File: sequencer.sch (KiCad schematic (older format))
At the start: 27 parts, among them J101 USB_A, J102 NHD-3.12-25664UC, J103 PJS008U-3000, U101 74HCT125, U102 74HC595, U103 74HC595, U104 74HC595, U105 74HC165

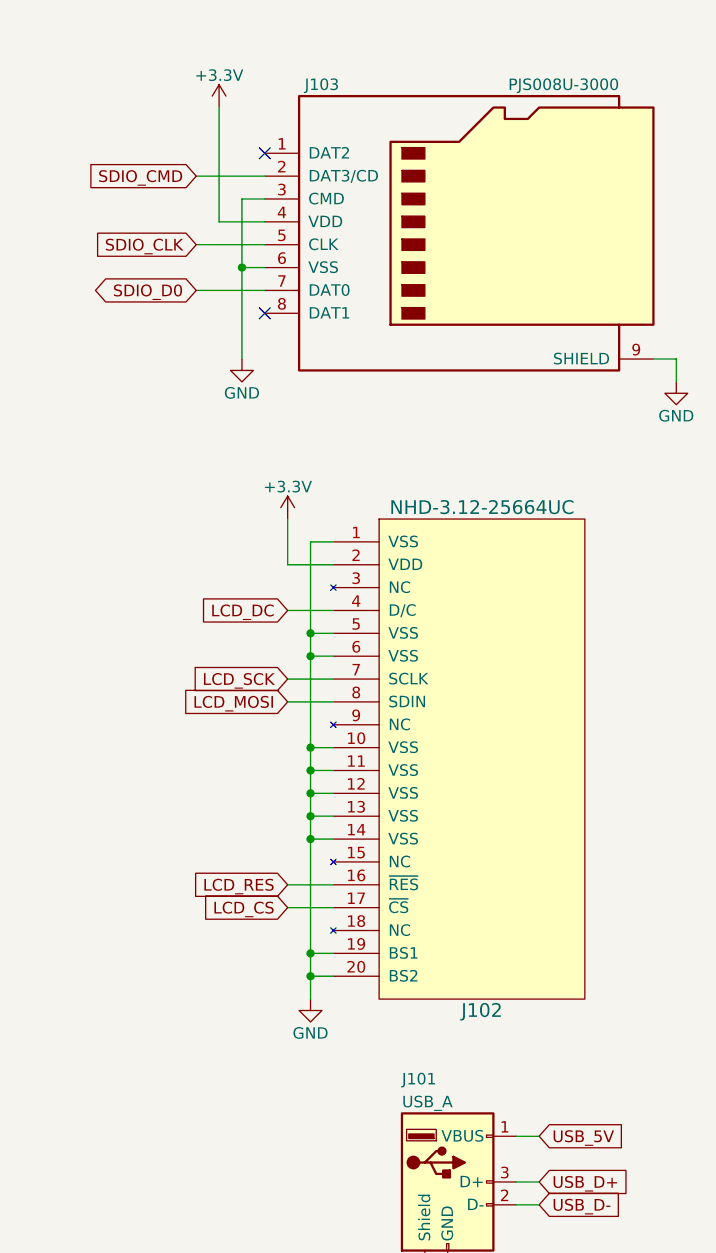
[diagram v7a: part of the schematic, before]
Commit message: renamed header references to JPxxx
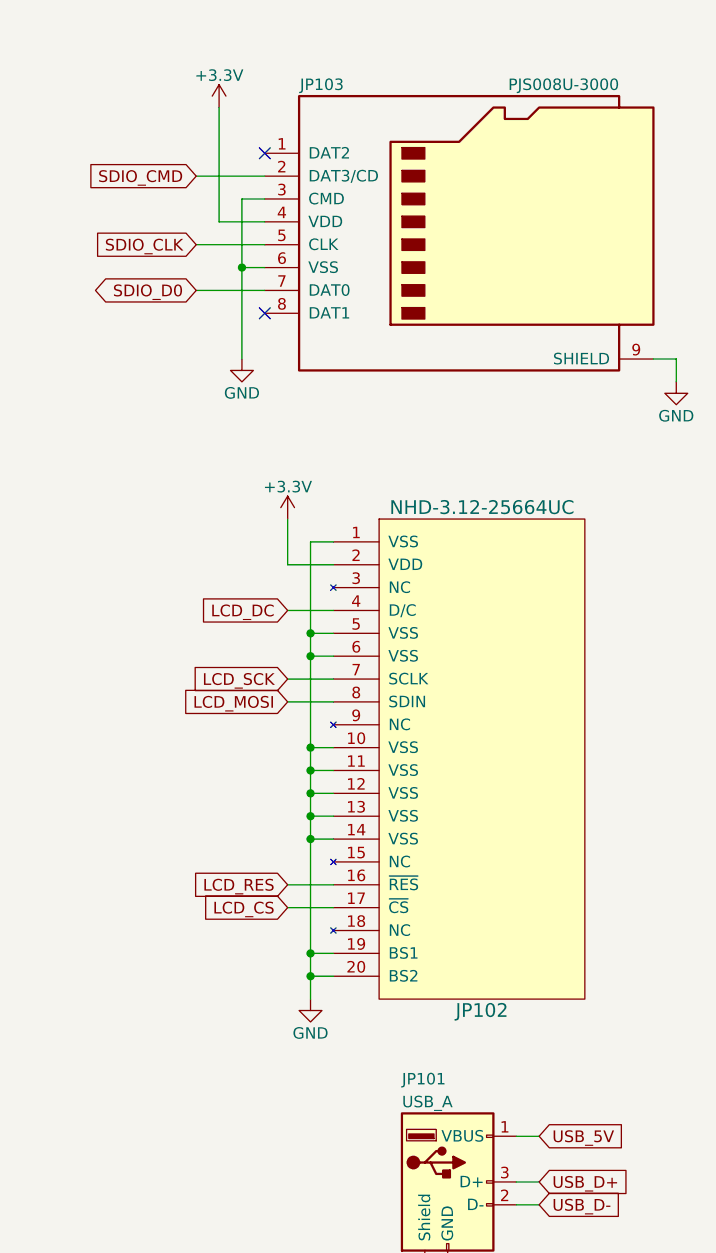
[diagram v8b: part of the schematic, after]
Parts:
- renumbered J101 to JP101, J102 to JP102, J103 to JP103
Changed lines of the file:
@@
 $EndComp
 $Comp
-L NHD-3.12-25664UC J102
+L NHD-3.12-25664UC JP102
 U 1 1 59DBF1B1
 P 9500 2800
-F 0 "J102" H 10150 750 60  0000 C CNN
+F 0 "JP102" H 10150 750 60  0000 C CNN
 F 1 "NHD-3.12-25664UC" H 10150 2950 60  0000 C CNN
 F 2 "w_lcd:NHD-3.12-25664UC" H 9700 3000 60  0001 C CNN
@@
 $EndComp
 $Comp
-L Micro_SD_Card J103
+L Micro_SD_Card JP103
 U 1 1 59DC0C9C
 P 10100 1400
-F 0 "J103" H 9450 2000 50  0000 C CNN
+F 0 "JP103" H 9450 2000 50  0000 C CNN
 F 1 "PJS008U-3000" H 10750 2000 50  0000 R CNN
 F 2 "w_connector:PJS008U-3000-0" H 11250 1700 50  0001 C CNN
@@
 $EndComp
 $Comp
-L USB_A J101
+L USB_A JP101
 U 1 1 59DE5EB2
 P 10000 5600
-F 0 "J101" H 9800 6050 50  0000 L CNN
+F 0 "JP101" H 9800 6050 50  0000 L CNN
 F 1 "USB_A" H 9800 5950 50  0000 L CNN
 F 2 "w_connector:MOLEX_USB_105057" H 10150 5550 50  0001 C CNN
